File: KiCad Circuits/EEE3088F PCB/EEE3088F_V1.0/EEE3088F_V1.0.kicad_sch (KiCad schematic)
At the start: 60 parts, among them J1 Conn_01x02_Pin, J2 Conn_02x16_Odd_Even, U1 MT3608, U10 HX SS12D10G6-WJ, U11 HUSB237-AA001-DN06R, U2 INA219AxD, U3 DRV8833PWP, U4 AP2112K-3.3, U5 DRV8833PWP, U6 BQ24074RGT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

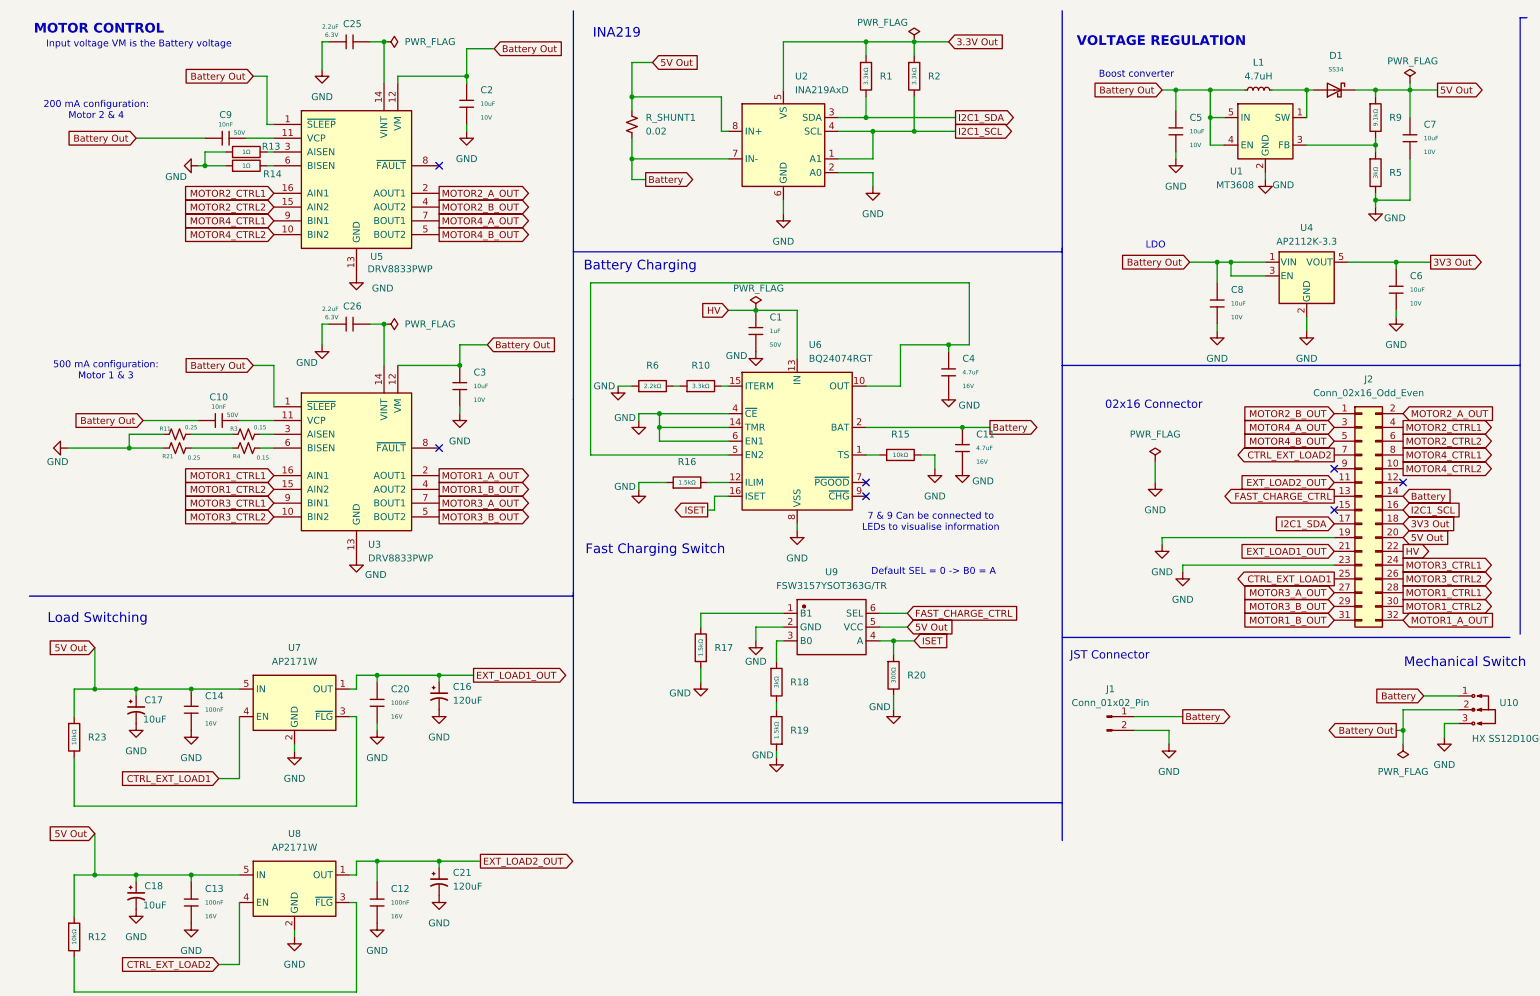
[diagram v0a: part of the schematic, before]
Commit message: Updated components, started PCB
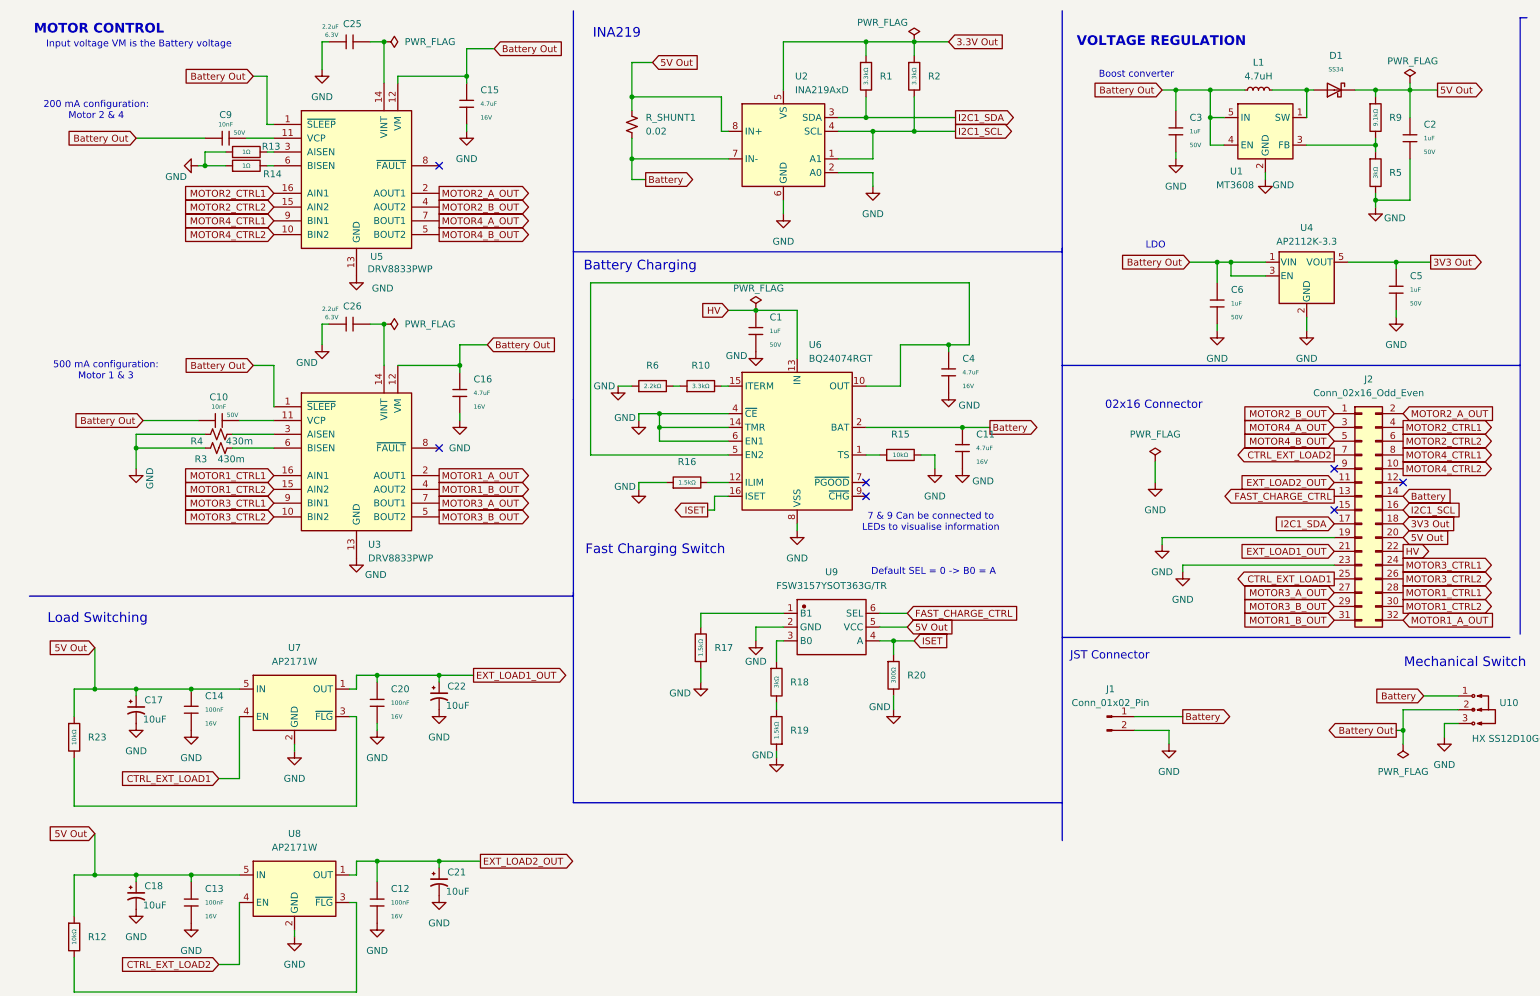
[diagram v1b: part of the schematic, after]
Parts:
- removed C16: 120uF, Footprints:CAP-TH_BD8.0-P3.50-D0.6-FD, symbol Device:C_Polarized_Small_US
- removed C2, C3, C5, C6, C7, C8: 10uF, PCM_JLCPCB:C_0603, symbol PCM_JLCPCB-Capacitors:0603,10uF
- removed R11, R21: 0.25, Footprints:R1206, symbol Device:R_Small_US
- added C15, C16: 4.7uF, PCM_JLCPCB:C_0603, symbol PCM_JLCPCB-Capacitors:0603,4.7uF
- added C2, C3, C5, C6: 1uF, PCM_JLCPCB:C_0603, symbol PCM_JLCPCB-Capacitors:0603,1uF
- added C22: 10uF, Footprints:CAP-TH_BD5.0-P2.00-D0.8-FD, symbol Device:C_Polarized_Small_US
- C21: value 120uF -> 10uF; footprint Footprints:CAP-TH_BD8.0-P3.50-D0.6-FD -> Footprints:CAP-TH_BD5.0-P2.00-D0.8-FD
- R3, R4: value 0.15 -> 430m; footprint Footprints:R0603 -> Footprints:R1206
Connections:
- net 3V3 Out: now also C5.1
- net 5V Out: now also C2.1
- net Battery Out: now also C15.1, C16.1, C3.1, C6.1
- net EXT_LOAD1_OUT: now also C22.1
- net GND: now also R3.1, R4.1, C15.2, C16.2, C2.2, C22.2, C3.2, C5.2, C6.2
- net at R3.2: now also U3.6 (BISEN); no longer U3.3 (AISEN)
- net at R4.2: now also U3.3 (AISEN); no longer U3.6 (BISEN)

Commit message: Updated the Kicad pcb
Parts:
- removed C19: 10uF, PCM_JLCPCB:C_0603, symbol PCM_JLCPCB-Capacitors:0603,10uF
- added C19: 1uF, PCM_JLCPCB:C_0603, symbol PCM_JLCPCB-Capacitors:0603,1uF
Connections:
- net GND: now also C19.2
- net HV: now also U11.2 (VUSB), USB1.A9 (VBUS), USB1.B9 (VBUS), C19.1
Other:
- moved on the sheet: R22, U10, U11, USB1

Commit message: Edited Kicad
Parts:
- U1: footprint Footprints:SOT-23-5_L3.0-W1.7-P0.95-LS2.8-BR -> PCM_JLCPCB:SOT-23-5_L3.0-W1.7-P0.95-LS2.8-BR
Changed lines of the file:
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@@
 			)
 		)
-		(property "Footprint" "Footprints:SOT-23-5_L3.0-W1.7-P0.95-LS2.8-BR"
+		(property "Footprint" "PCM_JLCPCB:SOT-23-5_L3.0-W1.7-P0.95-LS2.8-BR"
 			(at 241.3 40.64 0)
 			(effects

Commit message: added test points
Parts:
- added TP1, TP10, TP12, TP2, TP4, TP5, TP6, TP7, TP8, TP9: TestPoint, TestPoint:TestPoint_Pad_4.0x4.0mm, symbol Connector:TestPoint
- added TP17, TP18, TP21: TestPoint_2Pole, TestPoint:TestPoint_Bridge_Pitch5.08mm_Drill1.3mm, symbol Connector:TestPoint_2Pole
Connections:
- net 3.3V Out: now also TP7.1
- net 3V3 Out: now also TP4.1
- net 5V Out: now also TP10.1, TP2.1, TP5.1
- net Battery: now also TP6.1, TP9.1
- net Battery Out: now also TP1.1
- net EXT_LOAD1_OUT: now also TP21.1, TP21.2
- net HV: now also TP12.1, TP8.1
- net MOTOR3_B_OUT: now also TP17.1, TP17.2
- net MOTOR4_B_OUT: now also TP18.1, TP18.2
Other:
- note added: "ISET used to control the charging current"
- note added: "Motor Control"
- note added: "Requirement 1"
- note added: "Requirement 2"
- note added: "Requirement 3 and Requirement 4"
- note added: "Requirement 5"
- note added: "Requirement 6"
- note added: "Requirement 7"
- note added: "Requirement 8"
- note removed: "Input voltage VM is the Battery voltage"
- note removed: "MOTOR CONTROL"
- moved on the sheet: C1, C10, C11, C12, C13, C14, C15, C16, C17, C18, C19, C2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

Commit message: Final PCB
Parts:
- removed TP17, TP18, TP21: TestPoint_2Pole, TestPoint:TestPoint_Bridge_Pitch5.08mm_Drill1.3mm, symbol Connector:TestPoint_2Pole
